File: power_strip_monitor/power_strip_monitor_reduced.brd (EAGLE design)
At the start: 80 x 55 mm, 72 parts, among them Q1 4.096MHz, U1 CS5467, U2 CS5467, U4 ATMEGA168, U5 RAC01_02-SC, U6 XBEE-1B1

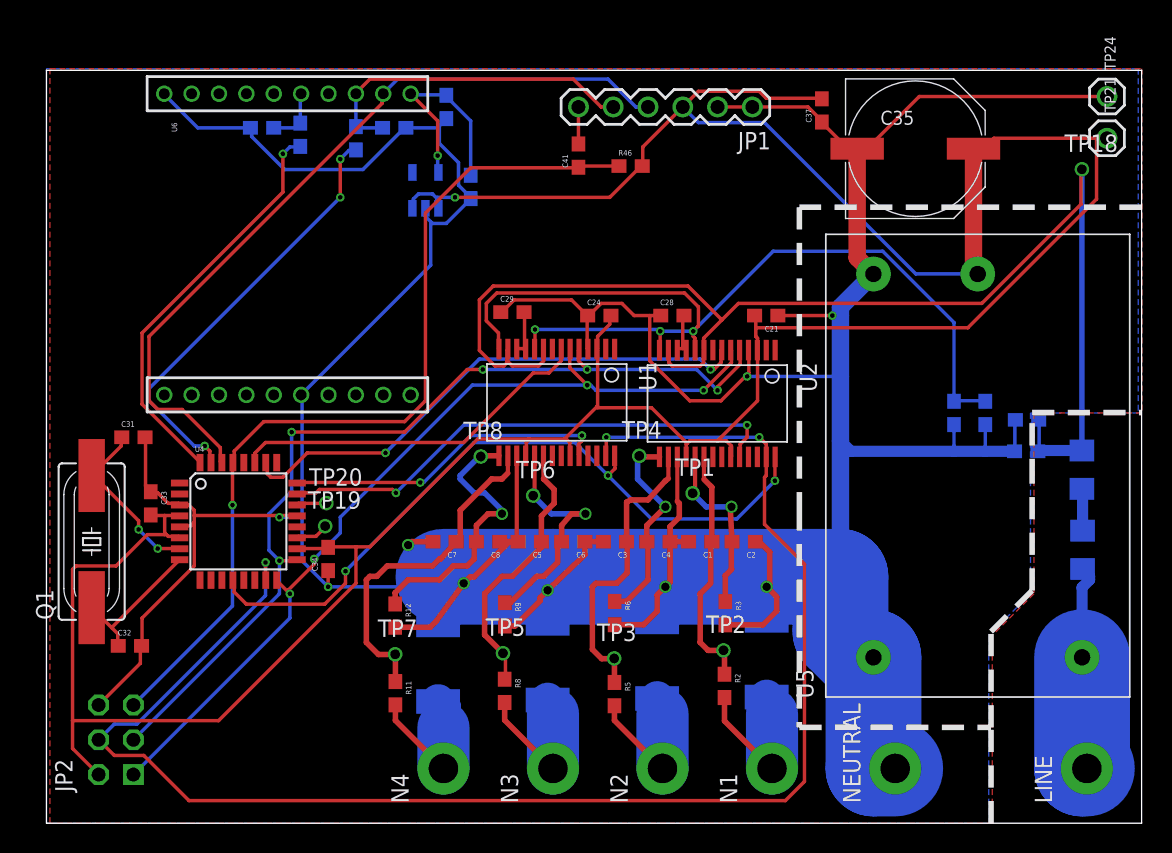
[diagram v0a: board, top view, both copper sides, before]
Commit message: Added LEDs on schematic and layout
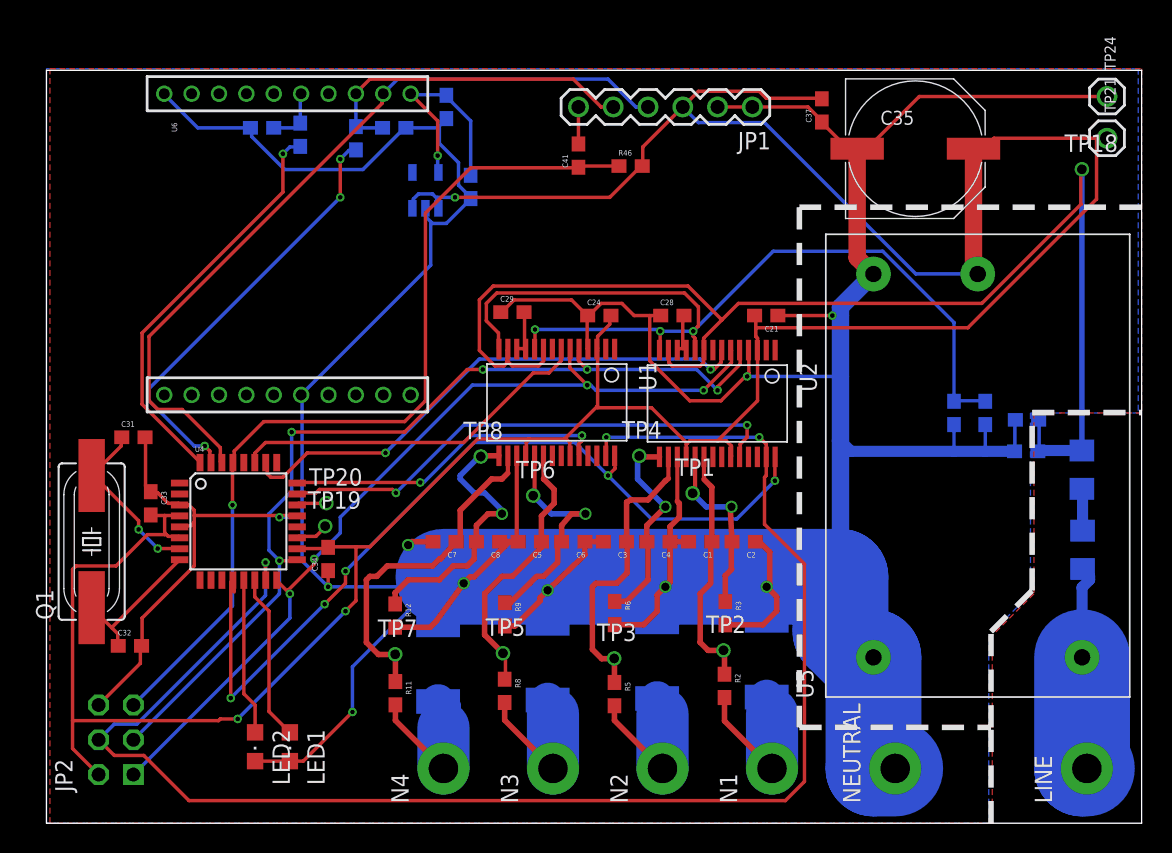
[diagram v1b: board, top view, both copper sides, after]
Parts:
- added LED1, LED2: (no value), led:CHIPLED_0805
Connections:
- new net N$1: LED2.A, U4.13
- new net N$3: LED1.A, U4.14
- net GND: now also LED1.C, LED2.C
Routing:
- net GND: track 372.1 -> 387.4 mm, vias 9 -> 10
- net N$3: track 0.00 -> 12.2 mm
- net N$1: track 0.00 -> 11.5 mm
- net XIN: track 53.1 -> 64.5 mm, vias 3 -> 5
- net 5V: track 230.9 -> 231.6 mm, vias 1 -> 3
